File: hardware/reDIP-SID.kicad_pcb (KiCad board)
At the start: 4 copper layers, 17.8 x 35.6 mm, 90 parts, among them J1 Conn_01x04, J2 Conn_01x04, J3 Conn_01x10, J4 Conn_01x10, J5 TYPE-C-31-M-12, J6 Conn_02x05_Odd_Even, SW1 KXT331LHS, U1 NCP115AMX120TCG, U2 NCP167AMX330TBG, U3 SN74CBTD16211DGVR, U4 SGTL5000XNLA3, U5 NUF2042XV6, U6 APS6404L-3SQR-SN, U7 W25Q128JVPIM, U8 ICE40UP5K-SG48I, X1 ECS-1612MV-240-CN-TR

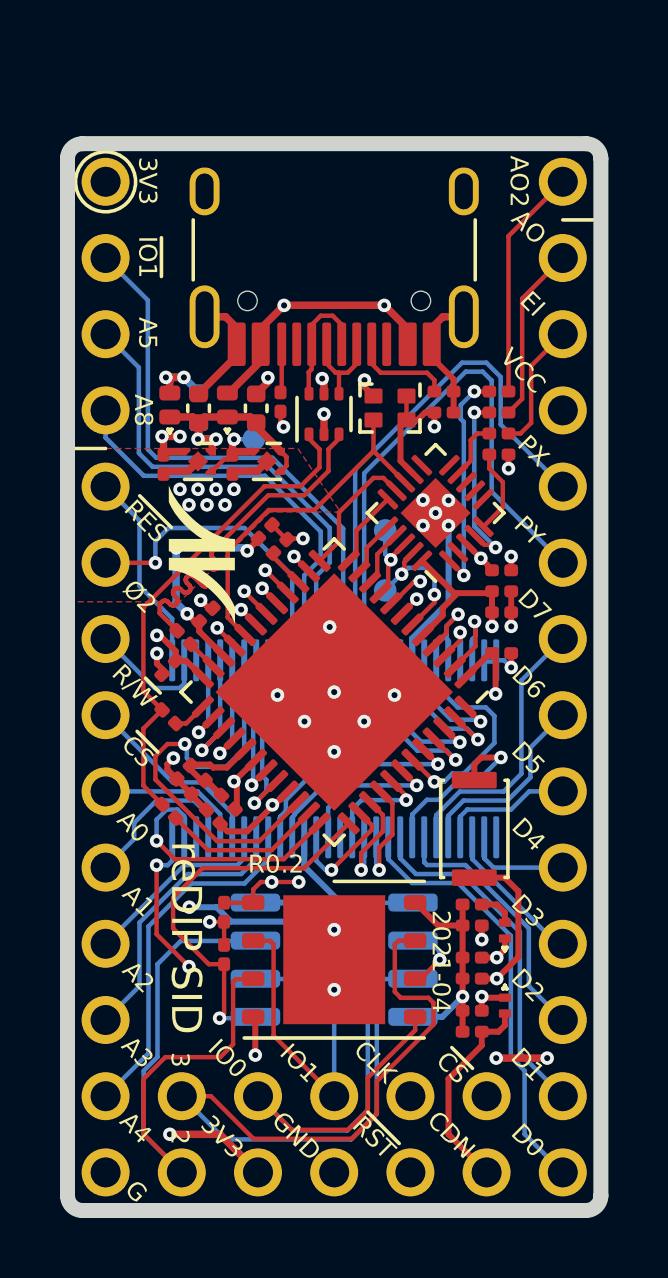
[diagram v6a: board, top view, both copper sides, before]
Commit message: Revision 1.0
This revision rounds off the features of the board, both as a drop-in
SID replacement, and as a generic FPGA platform for audio and / or 5V
tolerant I/O:

* Fully 6581 / 8580 pin compatible
* Machined (round) socket pin headers, for mounting directly in a SID socket
* C64 model detection by measurement of VDD on SGTL5000 MIC input
* DC bias for SID audio output, required by C64 audio output stage
* Hardware mixing of left and right audio channels into SID audio output
* Stereo outputs, in addition to mono SID audio output
* Stereo inputs
* Schottky diodes replaced with power switch, minimizing 5V rail voltage drop
* Separate LDO for SGTL5000 VDDD, avoiding overvoltage on iCE40 VCC
* USB-C receptacle footprint adjustments, for compatibility with both
  HRO TYPE-C-31-M-12 and GCT USB4105
* USB-C receptacle flush with board edge
* Button force changed from 240gf to 100gf
* Blue CDONE LED dimmed down a bit
* Solder mask color changed to matte black

All known issues with the first prototype (r0.2) have been fixed.

Special thanks to @smunaut for invaluable help!
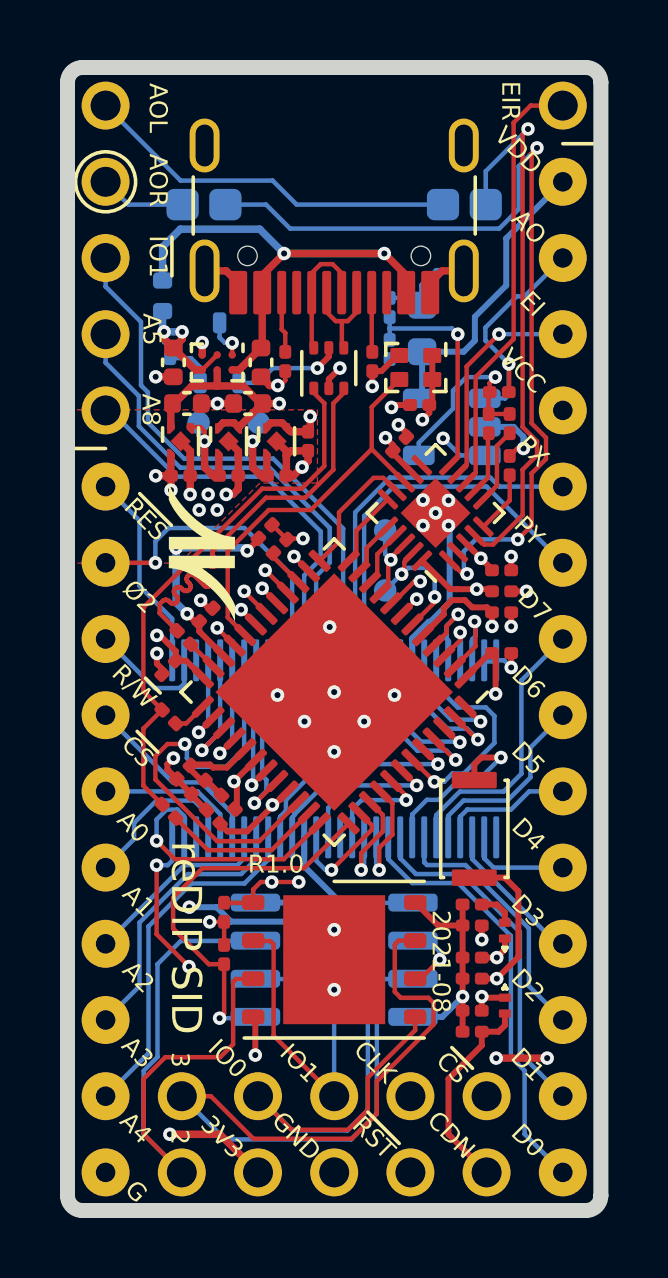
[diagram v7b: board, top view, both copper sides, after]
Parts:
- removed the C10 at (113.1, 107.7)
- removed the D2 at (102.1, 107.4)
- removed the J4 at (115.2, 110.2)
- removed the R4 at (105.8, 107.3)
- removed SolderMask D0.5mm: SolderMask_D0.5mm, reDIP:SolderMask_D0.5mm (x14)
- removed SolderMask D0.5mm: SolderMask_D0.3mm, reDIP:SolderMask_D0.3mm (x7)
- added C13: 1uF, Capacitor_SMD:C_0603_1608Metric, B.Cu at (110.5, 104.9)
- added C14: 10uF, Capacitor_Tantalum_SMD:CP_EIA-1608-08_AVX-J, B.Cu at (103.3, 100.8)
- added C25: 0.1uF, Capacitor_SMD:C_0201_0603Metric, F.Cu at (110.5, 107.4)
- added C5: 1uF, Capacitor_SMD:C_0402_1005Metric, F.Cu at (102.7, 107.4)
- added C6: 1uF, Capacitor_SMD:C_0201_0603Metric, F.Cu at (102.5, 109.8)
- added C7: 1uF, Capacitor_SMD:C_0201_0603Metric, F.Cu at (106.8, 108.7)
- added J3: Conn_01x14, reDIP:PinHeader_1x14_P2.54mm_Vertical_Machined, B.Cu at (115.2, 100.0)
- added R1: 20k, Resistor_SMD:R_0201_0603Metric, B.Cu at (102.2, 106.2)
- added R10: 5.1k, Resistor_SMD:R_0201_0603Metric, F.Cu at (106.0, 106.0)
- added R13: 10k, Resistor_SMD:R_0201_0603Metric, F.Cu at (105.3, 111.7)
- added R5: 402k, Resistor_SMD:R_0201_0603Metric, B.Cu at (109.5, 105.6)
- added R6: 20k, Resistor_SMD:R_0201_0603Metric, F.Cu at (112.8, 108.1)
- added R8: 100k, Resistor_SMD:R_0201_0603Metric, B.Cu at (109.5, 104.2)
- added R9: 10k, Resistor_SMD:R_0201_0603Metric, F.Cu at (113.1, 107.0)
- added SolderMask_D0.3mm: SolderMask_D0.3mm, reDIP:SolderMask_D0.3mm, B.Cu at (107.6, 119.0)
- added SolderMask_D0.3mm: SolderMask_D0.3mm, reDIP:SolderMask_D0.3mm, F.Cu at (104.0, 110.4)
- added SolderMask_D0.3mm: SolderMask_D0.3mm, reDIP:SolderMask_D0.3mm, F.Cu at (103.4, 110.4)
- added SolderMask_D0.3mm: SolderMask_D0.3mm, reDIP:SolderMask_D0.3mm, F.Cu at (102.8, 110.4)
- added SolderMask_D0.3mm: SolderMask_D0.3mm, reDIP:SolderMask_D0.3mm, B.Cu at (108.6, 118.0)
- added SolderMask_D0.3mm: SolderMask_D0.3mm, reDIP:SolderMask_D0.3mm, B.Cu at (106.6, 118.0)
- added SolderMask_D0.3mm: SolderMask_D0.3mm, reDIP:SolderMask_D0.3mm, B.Cu at (109.6, 117.1)
- added SolderMask_D0.3mm: SolderMask_D0.3mm, reDIP:SolderMask_D0.3mm, B.Cu at (107.6, 117.0)
- added SolderMask_D0.3mm: SolderMask_D0.3mm, reDIP:SolderMask_D0.3mm, B.Cu at (105.7, 117.1)
- added SolderMask_D0.3mm: SolderMask_D0.3mm, reDIP:SolderMask_D0.3mm, B.Cu at (107.5, 114.8)
- added SolderMask_D0.3mm: SolderMask_D0.3mm, reDIP:SolderMask_D0.3mm, F.Cu at (103.7, 110.9)
- added SolderMask_D0.3mm: SolderMask_D0.3mm, reDIP:SolderMask_D0.3mm, F.Cu at (103.1, 110.9)
- added SolderMask_D0.5mm: SolderMask_D0.5mm, reDIP:SolderMask_D0.5mm, B.Cu at (103.1, 110.9)
- added SolderMask_D0.5mm: SolderMask_D0.5mm, reDIP:SolderMask_D0.5mm, B.Cu at (102.8, 110.4)
- added SolderMask_D0.5mm: SolderMask_D0.5mm, reDIP:SolderMask_D0.5mm, B.Cu at (103.4, 110.4)
- added SolderMask_D0.5mm: SolderMask_D0.5mm, reDIP:SolderMask_D0.5mm, B.Cu at (103.7, 110.9)
- added SolderMask_D0.5mm: SolderMask_D0.5mm, reDIP:SolderMask_D0.5mm, B.Cu at (104.0, 110.4)
- added TP2: TestPoint_Flag, reDIP:TestPoint_Pad_D0.75mm, B.Cu at (105.1, 108.0)
- added U3: NCP115AMX120TCG, ONSemi:CASE_711AJ_1.0x1.0mm_P0.65mm, F.Cu at (105.7, 108.7)
- added U4: FPF1321UCX, ONSemi:CASE567RM_1.46x0.96mm_P0.5mm, F.Cu at (103.7, 106.0)
- added U8: MCP6H01T-E/OT, reDIP:SOT-23-5, B.Cu at (111.5, 108.2)
- added svg2mod: G***, reDIP:Nimrod-N, B.Cu at (108.6, 108.5)
- C15: value 1uF -> 10uF; footprint Capacitor_SMD:C_0201_0603Metric -> Capacitor_Tantalum_SMD:CP_EIA-1608-08_AVX-J; moved to B.Cu
- C2: footprint Capacitor_SMD:C_0201_0603Metric -> Capacitor_SMD:C_0402_1005Metric
- C9: value 1uF -> 0.1uF
- D1: value PMEG2010BELD -> BAV70W; footprint Nexperia:D_SOD-882D -> reDIP:SOT-323_SC-70; moved to B.Cu
- J1: value Conn_01x04 -> Conn_01x01; footprint reDIP:PinHeader_1x04_P2.54mm_Vertical_LongTail -> reDIP:PinHeader_1x01_P2.54mm_Vertical; moved to F.Cu
- J2: value Conn_01x04 -> Conn_01x05; footprint reDIP:PinHeader_1x04_P2.54mm_Vertical_LongTail -> reDIP:PinHeader_1x05_P2.54mm_Vertical; moved to F.Cu
- J4: renamed from J3; footprint reDIP:PinHeader_1x10_P2.54mm_Vertical -> reDIP:PinHeader_1x10_P2.54mm_Vertical_Machined
- R14: renamed from R8; value 1.5k -> 2.2k
- R7: value 10k -> 20k
- SW1: value KXT331LHS -> KXT311LHS
- SolderMask_D0.5mm (x7): renamed from SolderMask D0.5mm
- U9: renamed from U6; value APS6404L-3SQR-SN -> LY68L6400SLIT
- X1: value ECS-1612MV-240-CN-TR -> ASCO-24.000MHZ-EK-T3
- svg2mod: footprint reDIP:Nimrod-logo -> reDIP:Nimrod-text
- moved J1 15.5 mm to (115.2, 97.5), turned to 0 degrees
- moved J2 15.5 mm to (100.0, 97.5), turned to 0 degrees
- moved C15 13.6 mm to (112.0, 100.8), turned to 180 degrees
- moved R7 8.91 mm to (113.5, 108.1), turned to 270 degrees
- moved C8 7.54 mm to (105.7, 109.8)
- moved C9 6.66 mm to (113.2, 113.7), turned to 0 degrees
- moved JP1 3.92 mm to (101.9, 103.8), turned to 90 degrees
- moved C2 3.53 mm to (105.2, 106.0)
- moved C1 3.16 mm to (102.3, 106.0), turned to 270 degrees
- moved svg2mod 2.78 mm to (112.3, 112.5)
- moved R11 2.59 mm to (108.9, 106.0), turned to 90 degrees
- moved C4 2.20 mm to (104.1, 109.8), turned to 0 degrees
- moved TP1 1.88 mm to (103.1, 108.1)
- moved C10 1.81 mm to (109.8, 108.7), turned to 45 degrees
- moved D1 1.76 mm to (103.8, 105.7)
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- renumbered C5 to C10, C6 to C11, C7 to C12, C11 to C16, C12 to C17, C13 to C18, C14 to C19, C16 to C20, C17 to C21, C18 to C22, C19 to C23, C20 to C24, D3 to D2, D4 to D3, R5 to R11, R6 to R12, R9 to R15, R10 to R16, R11 to R17, R12 to R18, R13 to R19, R1 to R2, R14 to R20, R2 to R3, R3 to R4, TP2 to TP3, TP3 to TP4, U7 to U10, U8 to U11, U3 to U5, U4 to U6, U5 to U7
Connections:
- C1 pad 1: +5V -> VCC
- C15 pad 1: +1V2 -> Net-(C15-Pad1)
- C15 pad 2: GND -> /AOUT_L
- C2 pad 1: +1V2 -> VBUS
- C4 pad 1: +3V3 -> +1V2
- C8 pad 1: Net-(C8-Pad1) -> VDDD
- C8 pad 2: /EXT_IN -> GND
- C9 pad 1: /AUDIO_OUT_2 -> VDDD
- C9 pad 2: Net-(C9-Pad2) -> GND
- D1 pad 1: +5V -> VBUS
- D1 pad 2: VBUS -> VCC
- J1 pad 1: +3V3 -> /EXT_IN_R
- J2 pad 1: /AUDIO_OUT_2 -> /AOUT_L
- J2 pad 2: /AUDIO_OUT -> /AOUT_R
- J2 pad 3: /EXT_IN -> /~IO1~
- J2 pad 4: VCC -> /A5
- JP1 pad 2: +5V -> VBUS
- R7 pad 1: /SPI_SCLK -> Net-(R6-Pad1)
- R7 pad 2: +3V3 -> Net-(R7-Pad2)
- U6 pad 1: Net-(C9-Pad2) -> Net-(C14-Pad1)
- U6 pad 10: (no net) -> Net-(R5-Pad1)
- U6 pad 20: +1V2 -> VDDD
- U6 pad 4: Net-(C10-Pad2) -> Net-(C15-Pad1)
- U6 pad 6: (no net) -> Net-(R7-Pad2)
- U6 pad 7: (no net) -> Net-(R6-Pad2)
- U6 pad 8: (no net) -> /EXT_IN_R
- U6 pad 9: Net-(C8-Pad1) -> /EXT_IN
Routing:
- net Net-(C14-Pad1): track 0.00 -> 29.9 mm, vias 0 -> 3
- net Net-(C15-Pad1): track 0.00 -> 18.6 mm, vias 0 -> 1
- net VBUS: track 9.23 -> 26.7 mm
- net VDDD: track 0.00 -> 15.3 mm, vias 0 -> 2
- net /EXT_IN_R: track 0.00 -> 14.5 mm
- net /AOUT_L: track 0.00 -> 12.6 mm
- net VDD: track 0.00 -> 11.2 mm
- net GND: track 44.9 -> 55.1 mm, vias 36 -> 40
- net /AUDIO_OUT_2: track 7.75 -> 0.00 mm
- net Net-(R5-Pad1): track 0.00 -> 7.59 mm, vias 0 -> 1
- net Net-(C9-Pad2): track 7.55 -> 0.00 mm, vias 2 -> 0
- net Net-(R6-Pad1): track 0.00 -> 6.25 mm, vias 0 -> 1
- net /POT_Y: track 19.1 -> 12.9 mm
- net Net-(C10-Pad2): track 6.15 -> 0.00 mm, vias 2 -> 0
- net VCC: track 23.0 -> 28.6 mm
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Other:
- board size 17.8 x 35.6 mm -> 17.8 x 38.1 mm
- board text added: "2021-08"
- board text added: "38.10 mm"
- board text added: "AOL"
- board text added: "AOR"
- board text added: "EIR"
- board text added: "R1.0"
- board text added: "VDD"
- board text added: "VDDD"
- board text added: "tnt"
- board text removed: "1"
- board text removed: "2021-04"
- board text removed: "28"
- board text removed: "35.56 mm"
- board text removed: "AO2"
- board text removed: "No SID pins!"
- board text removed: "R0.2"
- board text removed: "pinout"

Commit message: Tweaks before manufacture
* Added test point for 5V rail
* Got rid of one BOM line by changing the MIC voltage divider
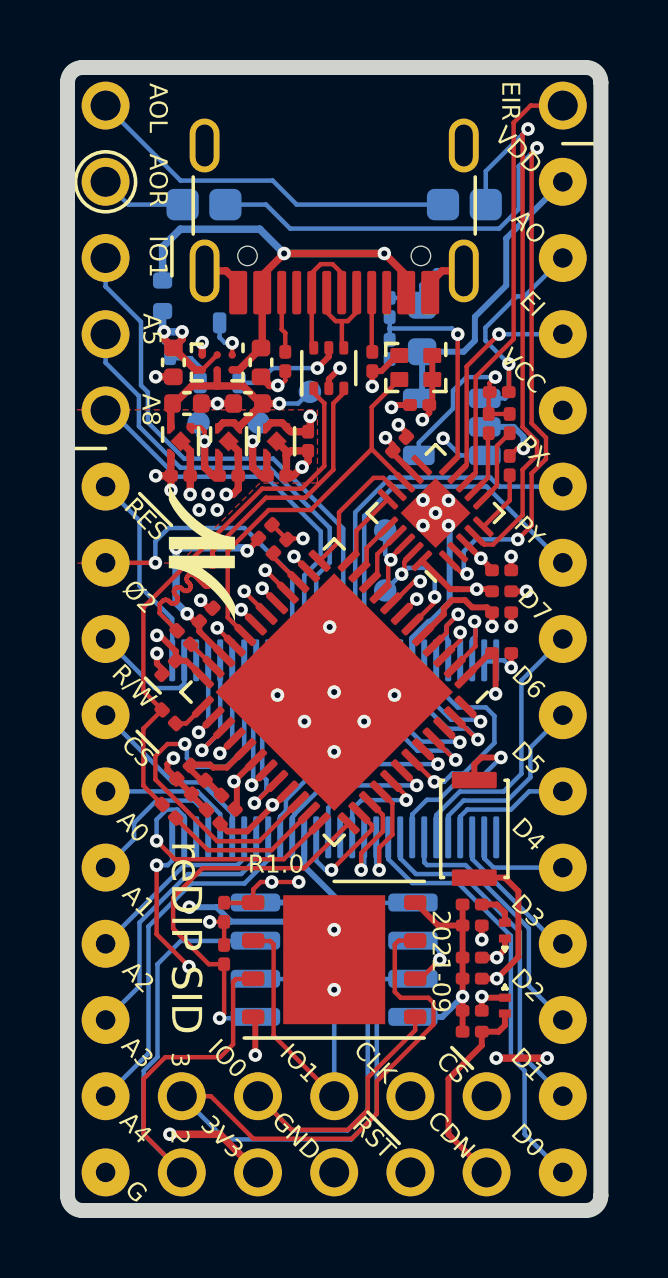
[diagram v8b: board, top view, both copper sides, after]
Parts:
- added TP3: TestPoint, reDIP:TestPoint_Pad_D0.75mm, B.Cu at (105.1, 108.0)
- R5: value 402k -> 100k
- R8: value 100k -> 20k
- TP1, TP2: value TestPoint_Flag -> TestPoint
- moved TP1 3.85 mm to (106.8, 107.0)
- moved TP2 2.02 mm to (103.1, 108.0)
- renumbered TP3 to TP4, TP4 to TP5
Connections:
- TP1 pad 1: +1V2 -> +5V
- TP2 pad 1: VDDD -> +1V2
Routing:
- net +5V: track 39.9 -> 41.1 mm
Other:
- board text added: "2021-09"
- board text added: "5V"
- board text removed: "2021-08"
